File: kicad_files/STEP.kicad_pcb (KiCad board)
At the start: 2 copper layers, 12 x 20 mm, 39 parts, among them Q1 AOCA32116E, U1 STM32WB55CEU6TR, U2 LSM6DSO32TR, U3 ANT016008LCS2442MA2, U4 BQ297xy, U5 TPS62840DLCR, Y1 NX1612SA-32.000MHZ-CHP-CIS-3

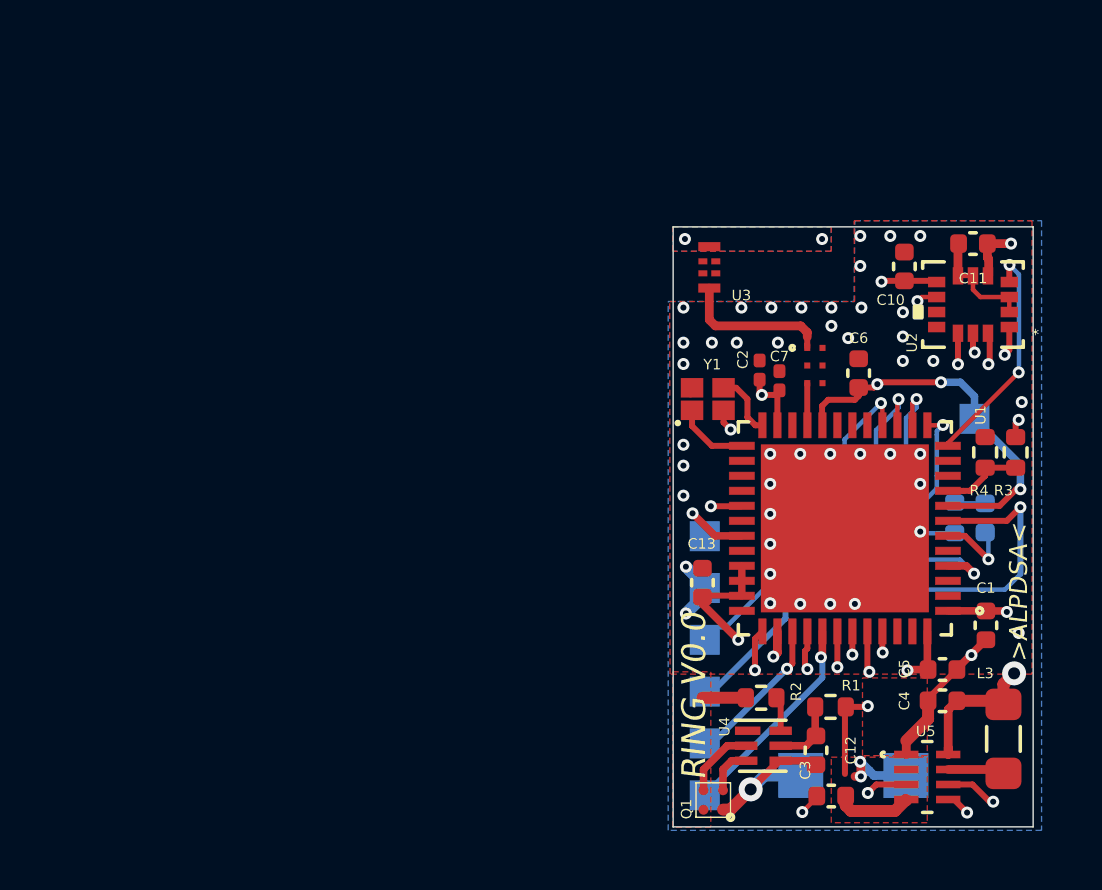
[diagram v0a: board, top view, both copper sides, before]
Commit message: finished v0.9 schematic and layout, annotated for review
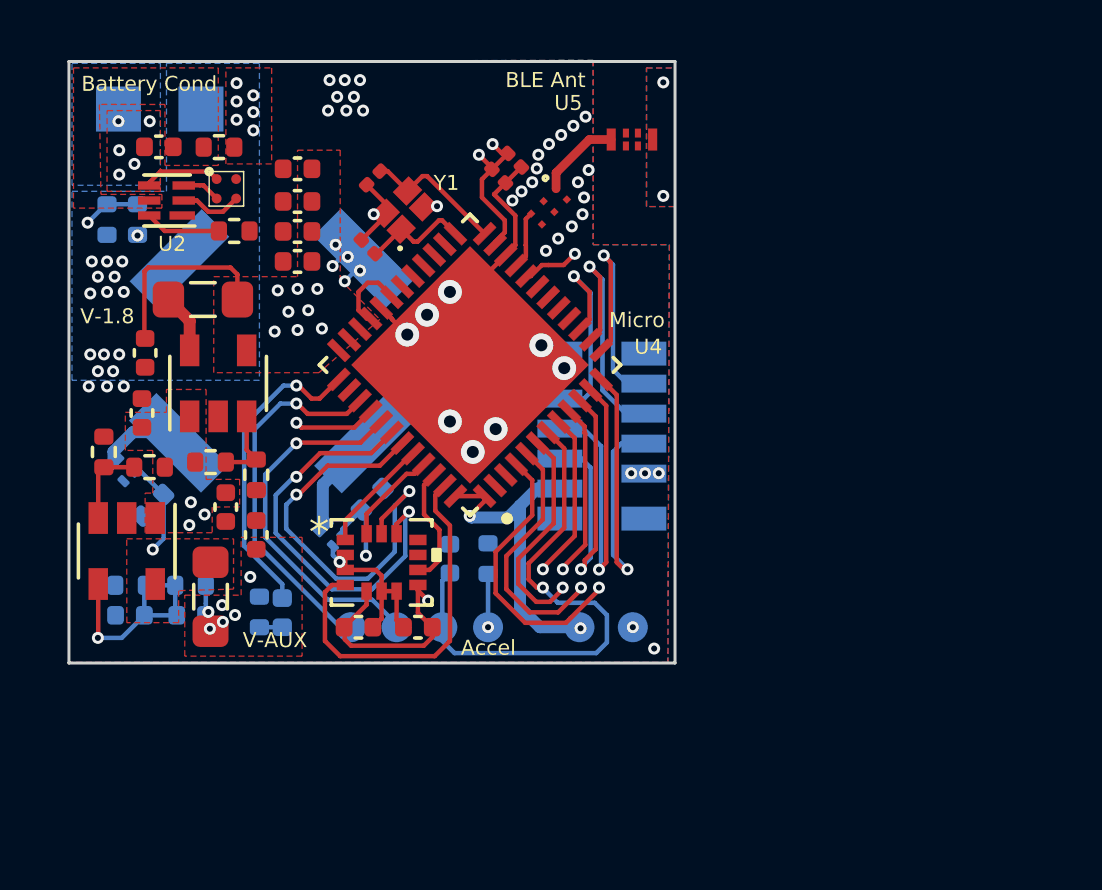
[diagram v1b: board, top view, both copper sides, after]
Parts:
- removed L3: L_2.2uH, Inductor_SMD:L_0805_2012Metric_Pad1.05x1.20mm_HandSolder
- removed TP10, TP11, TP12, TP13, TP9: Test_Point_SMD, TestPoint:TestPoint_Pad_1.0x1.0mm
- added C14: C_100nF, Capacitor_SMD:C_0402_1005Metric, F.Cu at (33.0, 32.0)
- added C15: C_4.7uF, Capacitor_SMD:C_0402_1005Metric, F.Cu at (30.6, 40.1)
- added C16: C_XF, Capacitor_SMD:C_0402_1005Metric, B.Cu at (29.5, 43.7)
- added C17: C_XF, Capacitor_SMD:C_0402_1005Metric, B.Cu at (27.4, 43.7)
- added C18: C_10uF, Capacitor_SMD:C_0402_1005Metric, F.Cu at (31.6, 41.1)
- added C8: C_100pF, Capacitor_SMD:C_0201_0603Metric, F.Cu at (35.5, 29.2)
- added C9: C_100nF, Capacitor_SMD:C_0402_1005Metric, F.Cu at (33.0, 28.9)
- added J1: CONN_FFC_FPC_VERT_8POS_0.5MM_SMD, step_footprints:tbf, B.Cu at (43.3, 37.8)
- added L1: L_2.2uH, Inductor_SMD:L_0805_2012Metric_Pad1.05x1.20mm_HandSolder, F.Cu at (29.9, 33.2)
- added L2: L_2.2uH, Inductor_SMD:L_0805_2012Metric_Pad1.05x1.20mm_HandSolder, F.Cu at (30.1, 43.1)
- added Q2: SSM3K35CTC, Package_TO_SOT_SMD:SOT-883, B.Cu at (34.1, 41.0)
- added Q3: SSM3K35CTC, Package_TO_SOT_SMD:SOT-883, B.Cu at (27.1, 38.9)
- added R10: R_10K, Resistor_SMD:R_0402_1005Metric, B.Cu at (39.4, 41.9)
- added R11: R_10K, Resistor_SMD:R_0402_1005Metric, B.Cu at (35.5, 39.9)
- added R12: R_10K, Resistor_SMD:R_0402_1005Metric, B.Cu at (28.2, 40.1)
- added R13: R_10k, Resistor_SMD:R_0402_1005Metric, F.Cu at (28.1, 38.8)
- added R14: R_X, Resistor_SMD:R_0402_1005Metric, F.Cu at (26.6, 38.3)
- added R15: R_10k, Resistor_SMD:R_0402_1005Metric, F.Cu at (30.1, 38.6)
- added R16: R_X, Resistor_SMD:R_0402_1005Metric, F.Cu at (31.6, 39.1)
- added R17: R_10k, Resistor_SMD:R_0402_1005Metric, B.Cu at (29.4, 42.7)
- added R18: R_X, Resistor_SMD:R_0402_1005Metric, B.Cu at (27.4, 42.7)
- added U6, U8: PKMCS0909E4000-R1, step_footprints:SPKR_PKMCS0909E4000-R1, B.Cu at (32.1, 34.9)
- added U7: LM3671TL-ADJ/NOPB, step_footprints:SOT-23-5, F.Cu at (27.3, 41.6)
- AE1: footprint step-footprints:MLPF-WB55-01E3 -> step_footprints:MLPF-WB55-01E3
- C1: value C_100nF -> C_4.7uF
- C11, C6: value C_100nF -> C_100pF; footprint Capacitor_SMD:C_0402_1005Metric -> Capacitor_SMD:C_0201_0603Metric
- C12: value C_0.1uF -> C_100nF
- C13: footprint Capacitor_SMD:C_0402_1005Metric -> Capacitor_SMD:C_0201_0603Metric
- C2: value C_100nF -> C_0.1uF; footprint Capacitor_SMD:C_0201_0603Metric -> Capacitor_SMD:C_0402_1005Metric
- C3: value C_4.7uF -> C_100nF
- C4: value C_10uF -> C_100nF
- C5: value C_100nF -> C_10uF
- C7: value C_100pF -> C_10nF; footprint Capacitor_SMD:C_0201_0603Metric -> Capacitor_SMD:C_0402_1005Metric; moved to B.Cu
- Q1: footprint step-footprints:AOCA32116E -> step_footprints:AOCA32116E
- R3, R4: moved to B.Cu
- TP1, TP2: footprint TestPoint:TestPoint_Pad_1.0x1.0mm -> TestPoint:TestPoint_Pad_1.5x1.5mm
- TP3, TP4, TP5, TP6: footprint TestPoint:TestPoint_Pad_1.0x1.0mm -> TestPoint:TestPoint_Pad_D1.0mm
- TP7, TP8: footprint TestPoint:TestPoint_Pad_1.5x1.5mm -> TestPoint:TestPoint_Pad_D1.0mm
- U1: value STM32WB55CEU6TR -> LSM6DSO32TR; footprint step-footprints:QFN50P700X700X60-49N -> step_footprints:LSM6DSO32TR
- U2: value LSM6DSO32TR -> BQ297xy; footprint step-footprints:LSM6DSO32TR -> Package_SON:WSON-6_1.5x1.5mm_P0.5mm
- U3: value ANT016008LCS2442MA2 -> LM3671TL-1V8/NOPB; footprint step-footprints:ANT016008LCS2442MA2 -> step_footprints:SOT-23-5
- U4: value BQ297xy -> STM32WB55CEU6TR; footprint Package_SON:WSON-6_1.5x1.5mm_P0.5mm -> step_footprints:QFN50P700X700X60-49N
- U5: value TPS62840DLCR -> ANT016008LCS2442MA2; footprint step-footprints:TPS62840DLCR -> step_footprints:ANT016008LCS2442MA2
- Y1: footprint step-footprints:OSCSC105P160X120X35-4N -> step_footprints:OSCSC105P160X120X35-4N
- moved R3 31.3 mm to (26.7, 30.6), turned to 90 degrees
- moved R4 29.3 mm to (27.7, 30.6), turned to -90 degrees
- moved C1 29.0 mm to (27.8, 37.0), turned to 90 degrees
- moved TP1 28.8 mm to (27.0, 26.9), turned to 180 degrees
- moved C5 28.6 mm to (27.9, 35.0), turned to -90 degrees
- moved TP2 28.4 mm to (29.8, 26.9), turned to 180 degrees
- moved R1 27.6 mm to (30.4, 28.1)
- moved U2 27.1 mm to (28.6, 29.9)
- moved Q1 26.5 mm to (30.3, 29.5), turned to -90 degrees
- moved C12 24.5 mm to (33.0, 31.0), turned to 180 degrees
- moved D1 23.6 mm to (32.5, 43.7), turned to 90 degrees
- moved R2 23.5 mm to (30.9, 30.9), turned to 180 degrees
- moved U5 23.4 mm to (44.2, 27.9), turned to 180 degrees
- moved R5 23.4 mm to (31.7, 43.6), turned to 90 degrees
- moved C2 21.4 mm to (28.4, 28.1), turned to 180 degrees
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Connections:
- AE1 pad 1: (no net) -> /RF_FILT
- AE1 pad 2: (no net) -> GND
- AE1 pad 3: (no net) -> /RF1
- AE1 pad 4: (no net) -> GND
- AE1 pad 5: (no net) -> GND
- AE1 pad 6: (no net) -> GND
- C1 pad 1: (no net) -> +BATT
- C1 pad 2: (no net) -> GND
- C10 pad 1: (no net) -> +1V8
- C10 pad 2: (no net) -> GND
- C11 pad 1: (no net) -> +1V8
- C11 pad 2: (no net) -> GND
- C12 pad 1: (no net) -> +1V8
- C12 pad 2: (no net) -> GND
- C13 pad 1: (no net) -> +1V8
- C13 pad 2: (no net) -> GND
- C2 pad 1: (no net) -> /BATT_FILT
- C2 pad 2: (no net) -> /CELL-
- C3 pad 1: (no net) -> +1V8
- C3 pad 2: (no net) -> GND
- C4 pad 1: (no net) -> +1V8
- C4 pad 2: (no net) -> GND
- C5 pad 1: (no net) -> +1V8
- C5 pad 2: (no net) -> GND
- C6 pad 1: (no net) -> /XTAL_FILT1
- C6 pad 2: (no net) -> GND
- C7 pad 1: (no net) -> /NRST
- C7 pad 2: (no net) -> GND
- D1 pad 1: (no net) -> Net-(D1-Pad1)
- D1 pad 2: (no net) -> /LED_DEBUG
- Q1 pad 1: (no net) -> /CELL-
- Q1 pad 2: (no net) -> GND
- Q1 pad 3: (no net) -> /C_GATE
- Q1 pad 4: (no net) -> /D_GATE
- R1 pad 1: (no net) -> /BATT_FILT
- R1 pad 2: (no net) -> +BATT
- R2 pad 1: (no net) -> GND
- R2 pad 2: (no net) -> /V_SENSE-
- R3 pad 1: (no net) -> +BATT
- R3 pad 2: (no net) -> /BATT_LVL
- R4 pad 1: (no net) -> /BATT_LVL
- R4 pad 2: (no net) -> GND
- R5 pad 1: (no net) -> Net-(D1-Pad1)
- R5 pad 2: (no net) -> GND
- TP1 pad 1: (no net) -> /CELL-
- TP2 pad 1: (no net) -> +BATT
- TP3 pad 1: (no net) -> /NRST
- TP4 pad 1: (no net) -> /SWDIO
- TP5 pad 1: (no net) -> /SWCLK
- TP6 pad 1: (no net) -> /BOOT0
- TP7 pad 1: (no net) -> +1V8
- TP8 pad 1: (no net) -> GND
- U1 pad 1: (no net) -> /MISO
- U1 pad 10: (no net) -> unconnected-(U1-Pad10)
- U1 pad 11: (no net) -> unconnected-(U1-Pad11)
- U1 pad 12: (no net) -> /CS
- U1 pad 13: (no net) -> /SCK
- U1 pad 14: (no net) -> /MOSI
- U1 pad 2: (no net) -> GND
- U1 pad 3: (no net) -> GND
- U1 pad 4: (no net) -> /LSM_INT1
- U1 pad 5: (no net) -> +1V8
- U1 pad 6: (no net) -> GND
- U1 pad 7: (no net) -> GND
- U1 pad 8: (no net) -> +1V8
- U1 pad 9: (no net) -> /LSM_INT2
- U2 pad 1: (no net) -> unconnected-(U2-Pad1)
- U2 pad 2: (no net) -> /C_GATE
- U2 pad 3: (no net) -> /D_GATE
- U2 pad 4: (no net) -> /CELL-
- U2 pad 5: (no net) -> /BATT_FILT
- U2 pad 6: (no net) -> /V_SENSE-
- U3 pad 1: (no net) -> +BATT
- U3 pad 2: (no net) -> GND
- U3 pad 3: (no net) -> /VEN_1V8
- U3 pad 4: (no net) -> +1V8
- U3 pad 5: (no net) -> /VSW_1V8
- U4 pad 1: (no net) -> +1V8
- U4 pad 2: (no net) -> unconnected-(U4-Pad2)
- U4 pad 3: (no net) -> unconnected-(U4-Pad3)
- U4 pad 4: (no net) -> /BOOT0
- U4 pad 5: (no net) -> /VBATT_BUZZER_LSD
- U4 pad 6: (no net) -> /VAUX_BUZZER_LSD
- U5 pad 1: (no net) -> /RAD_PLANE
- U5 pad 2: (no net) -> unconnected-(U5-Pad2)
- U5 pad 3: (no net) -> unconnected-(U5-Pad3)
- U5 pad 4: (no net) -> /RF_FILT
- U5 pad 5: (no net) -> unconnected-(U5-Pad5)
- U5 pad 6: (no net) -> unconnected-(U5-Pad6)
- Y1 pad 1: (no net) -> /XTAL_FILT1
- Y1 pad 2: (no net) -> GND
- Y1 pad 3: (no net) -> /XTAL_FILT3
- Y1 pad 4: (no net) -> GND
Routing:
- net (no net): track 180.9 -> 0.00 mm, vias 92 -> 0
- net +1V8: track 0.00 -> 48.3 mm, vias 0 -> 16
- net /BATT_LVL: track 0.00 -> 46.4 mm, vias 0 -> 3
- net /VAUX_BUZZER_LSD: track 0.00 -> 30.3 mm, vias 0 -> 2
- net /VBATT_BUZZER_LSD: track 0.00 -> 28.5 mm, vias 0 -> 2
- net GND: track 0.00 -> 21.0 mm, vias 0 -> 48
- net /NRST: track 0.00 -> 17.8 mm, vias 0 -> 1
- net /BOOT0: track 0.00 -> 17.2 mm, vias 0 -> 2
- net /SCK: track 0.00 -> 14.2 mm, vias 0 -> 2
- net /CS: track 0.00 -> 14.0 mm, vias 0 -> 2
- net /LSM_INT1: track 0.00 -> 12.5 mm
- net /SWCLK: track 0.00 -> 12.4 mm, vias 0 -> 1
- net /SWDIO: track 0.00 -> 12.3 mm, vias 0 -> 1
- net /ADC_IN_1: track 0.00 -> 12.1 mm, vias 0 -> 1
- net /ADC_IN_2: track 0.00 -> 12.0 mm, vias 0 -> 1
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- added copper zone on F.Cu, net +1V8
- added copper zone on In2.Cu, net +1V8
- added copper zone on B.Cu, net +BATT
- added copper zone on F.Cu, net +BATT
- added copper zone on In1.Cu, net +BATT
- added copper zone on F.Cu, net /BATT_FILT
- added copper zone on B.Cu, net /CELL-
- added copper zone on F.Cu, net /CELL-
- added copper zone on B.Cu, net /RAD_PLANE
- added copper zone on F.Cu, net /RAD_PLANE
- added copper zone on In1.Cu, net /RAD_PLANE
- added copper zone on In2.Cu, net /RAD_PLANE
- added copper zone on F.Cu, net /VSW_AUX
- added copper zone on B.Cu, net GND
- added copper zone on F.Cu, net GND
- added copper zone on In1.Cu, net GND
- added copper zone on In2.Cu, net GND
- added copper zone on F.Cu, net VAUX
- added copper zone on In1.Cu, net VAUX
- removed copper zone on B.Cu, net (none)
- removed copper zone on F.Cu, net (none)
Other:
- board size 12 x 20 mm -> 20.2 x 20.1 mm
- copper layers 2 -> 4
- board text added: "1.8V"
- board text added: "AUX Buzzer"
- board text added: "Accel"
- board text added: "BLE Ant"
- board text added: "Batt Buzzer"
- board text added: "Battery Cond"
- board text added: "CELL"
- board text added: "Haptic + Control Rev 0.9 - 3.10.23"
- board text added: "Micro"
- board text added: "NRST"
- board text added: "SWCLK"
- board text added: "SWDIO"
- board text added: "V-1.8"
- board text added: "V-AUX"
- board text added: "{dblquote}You have time to sleep when you're dead{dblquote}"
- board text removed: "1V8"
- board text removed: ">ALPDSA<"
- board text removed: "B0"
- board text removed: "B1"
- board text removed: "B2"
- board text removed: "B3"
- board text removed: "CLK"
- board text removed: "DIO"
- board text removed: "DNP"
- board text removed: "F ORII"
- board text removed: "RING V0.0"
- board text removed: "RST"
- board text removed: "[STEP AFTERHOURS]"
- board text removed: "~{NEON} RAINBOWS~{}"
- board text removed: "~{PCB} POLICE~{ }WAS HERE~{}"

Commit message: adjusted single via
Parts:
- C16: value C_XF -> C_YF
- R13, R15: value R_10k -> R_200k
- R14, R16: value R_X -> R_100k
- R17: value R_10k -> R_Y
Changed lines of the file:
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@@
       (effects (font (size 1 1) (thickness 0.15)))
     )
-    (fp_text value "R_X" (at 0 1.17 90) (layer "F.Fab")
+    (fp_text value "R_100k" (at 0 1.17 90) (layer "F.Fab")
       (effects (font (size 1 1) (thickness 0.15)))
     )
@@
       (effects (font (size 1 1) (thickness 0.15)))
     )
-    (fp_text value "R_X" (at 0 1.17 90) (layer "F.Fab")
+    (fp_text value "R_100k" (at 0 1.17 90) (layer "F.Fab")
       (effects (font (size 1 1) (thickness 0.15)))
     )
@@
       (effects (font (size 1 1) (thickness 0.15)))
     )
-    (fp_text value "R_10k" (at 0 1.17) (layer "F.Fab")
+    (fp_text value "R_200k" (at 0 1.17) (layer "F.Fab")
       (effects (font (size 1 1) (thickness 0.15)))
     )
@@
       (effects (font (size 1 1) (thickness 0.15)))
     )
-    (fp_text value "R_10k" (at 0 1.17) (layer "F.Fab")
+    (fp_text value "R_200k" (at 0 1.17) (layer "F.Fab")
       (effects (font (size 1 1) (thickness 0.15)))
     )
@@
       (effects (font (size 1 1) (thickness 0.15)) (justify mirror))
     )
-    (fp_text value "R_10k" (at 0 -1.17) (layer "B.Fab")
+    (fp_text value "R_Y" (at 0 -1.17) (layer "B.Fab")
       (effects (font (size 1 1) (thickness 0.15)) (justify mirror))
     )
@@
       (effects (font (size 1 1) (thickness 0.15)) (justify mirror))
     )
-    (fp_text value "C_XF" (at 0 -1.16) (layer "B.Fab")
-      (effects (font (size 1 1) (thickness 0.15)) (justify mirror))
-    )
+    (fp_text value "C_YF" (at 0 -1.16) (layer "B.Fab")
+      (effects (font (size 1 1) (thickness 0.15)) (justify mirror))
+    )

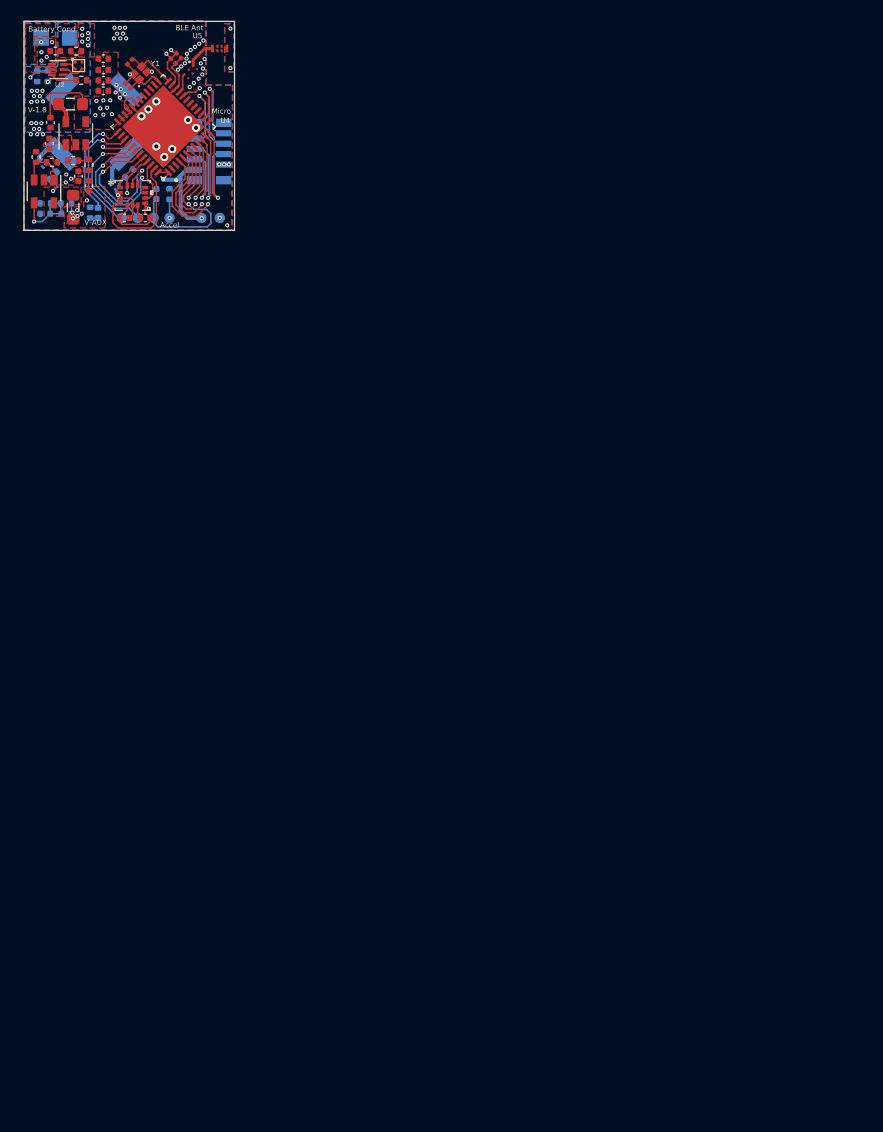
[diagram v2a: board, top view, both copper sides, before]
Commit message: post design review feedback, switching to external antenna for prototyping
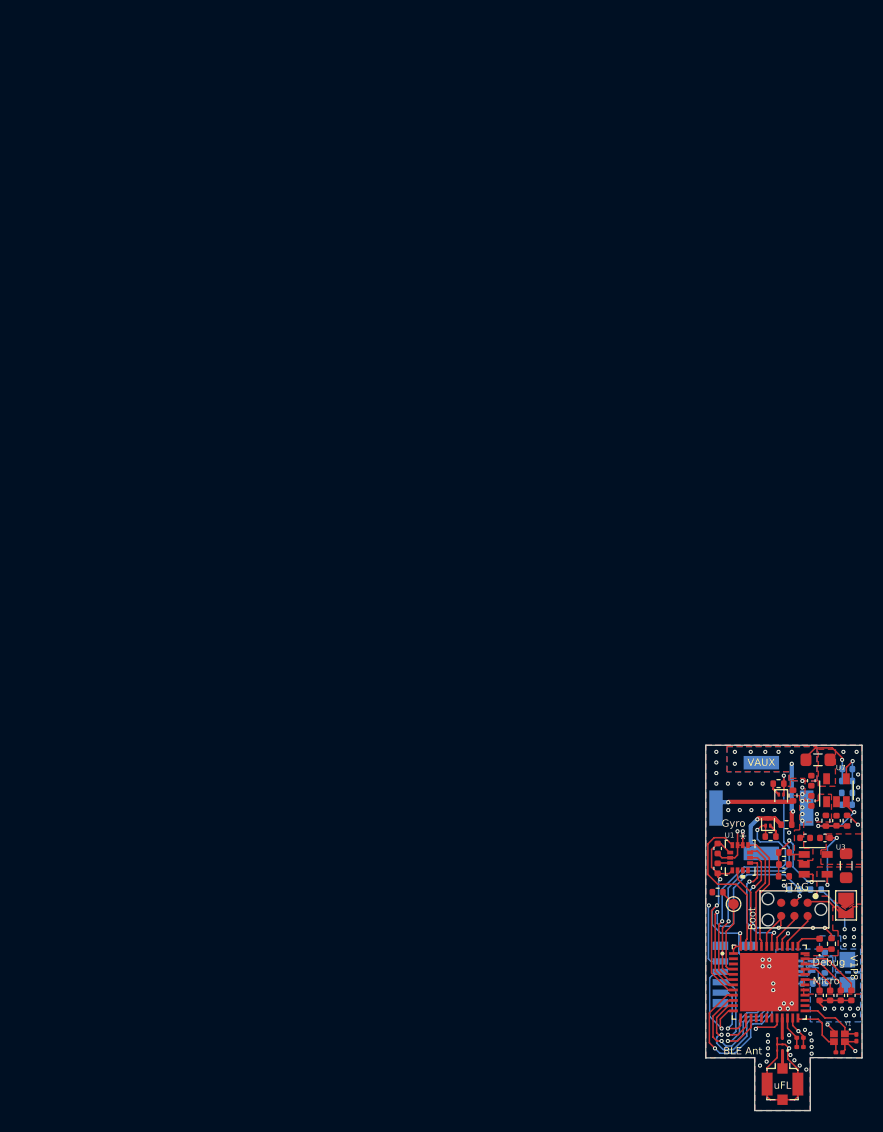
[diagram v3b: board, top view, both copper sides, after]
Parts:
- removed TP4, TP5, TP6, TP7, TP8: Test_Point_SMD, TestPoint:TestPoint_Pad_D1.0mm
- added C19: C_XF, Capacitor_SMD:C_0402_1005Metric, F.Cu at (103.3, 102.0)
- added C20: C_XF, Capacitor_SMD:C_0402_1005Metric, F.Cu at (98.3, 106.2)
- added J2: TC2030-IDC-TAGCONNECT, step_footprints:TAG_TC2030-IDC-NL, F.Cu at (99.3, 110.5)
- added R6: R_0, Jumper:SolderJumper-2_P1.3mm_Open_TrianglePad1.0x1.5mm, F.Cu at (104.3, 110.1)
- added R7: R_10K, Resistor_SMD:R_0402_1005Metric, F.Cu at (99.2, 99.6)
- added R8: R_10K, Resistor_SMD:R_0402_1005Metric, B.Cu at (101.4, 108.6)
- added R9: R_10K, Resistor_SMD:R_0402_1005Metric, F.Cu at (98.5, 102.4)
- C2, Q1, R1, R2, U2: moved to B.Cu
- D1, Q2, Q3, R10, R11, R12, R5, TP3: moved to F.Cu
- J1: value CONN_FFC_FPC_VERT_8POS_0.5MM_SMD -> Molex_FFC_FPC_VERT_8POS_0.5MM_SMD_0525590853
- U5: value ANT016008LCS2442MA2 -> Molex_Conn_uFL_0734120110; footprint step_footprints:ANT016008LCS2442MA2 -> Connector_Coaxial:U.FL_Molex_MCRF_73412-0110_Vertical
- moved TP2 117.6 mm to (104.4, 117.7)
- moved TP1 117.5 mm to (104.4, 115.3)
- moved C8 116.9 mm to (103.6, 124.2), turned to 0 degrees
- moved C6 115.0 mm to (105.3, 122.8), turned to -90 degrees
- moved C9 115.0 mm to (104.8, 118.7), turned to -90 degrees
- moved R1 114.3 mm to (102.2, 117.1), turned to -90 degrees
- moved Y1 114.3 mm to (103.6, 122.8), turned to 180 degrees
- moved R3 114.2 mm to (100.6, 117.6), turned to 180 degrees
- moved C2 114.1 mm to (102.2, 115.1), turned to 90 degrees
- moved C10 113.5 mm to (103.8, 118.7), turned to -90 degrees
- moved U5 113.1 mm to (98.2, 127.3)
- moved R4 112.5 mm to (98.6, 118.0), turned to 180 degrees
- moved C12 112.1 mm to (102.7, 118.7), turned to -90 degrees
- moved C11 112.1 mm to (99.9, 123.7), turned to 180 degrees
- moved U2 112.0 mm to (100.4, 115.9), turned to 0 degrees
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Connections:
- C5 pad 1: +1V8 -> /VFB_1V8
- L1 pad 2: +1V8 -> /VFB_1V8
- TP3 pad 1: /NRST -> /BOOT0
- U3 pad 4: +1V8 -> /VFB_1V8
- U4 pad 10: /ADC_IN_0 -> /ADC_IN_1
- U4 pad 11: /ADC_IN_1 -> /ADC_IN_0
- U5 pad 1: /RAD_PLANE -> /RF_FILT
- U5 pad 2: unconnected-(U5-Pad2) -> GND
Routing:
- net GND: track 21.0 -> 51.1 mm, vias 48 -> 57
- net /BATT_LVL: track 46.4 -> 19.7 mm, vias 3 -> 1
- net +1V8: track 48.3 -> 63.1 mm, vias 16 -> 12
- net VAUX: track 2.76 -> 12.7 mm, vias 11 -> 9
- net /SWCLK: track 12.4 -> 3.53 mm, vias 1 -> 0
- net /SWDIO: track 12.3 -> 3.64 mm, vias 1 -> 0
- net /BOOT0: track 17.2 -> 8.66 mm, vias 2 -> 0
- net /VEN_1V8: track 2.62 -> 10.5 mm, vias 0 -> 2
- net /LED_DEBUG: track 10.4 -> 2.57 mm, vias 1 -> 0
- net /MISO: track 3.83 -> 11.5 mm
- net /ADC_IN_0: track 10.7 -> 18.0 mm
- net /MOSI: track 3.25 -> 10.6 mm
- net /VFB_1V8: track 0.00 -> 6.55 mm, vias 0 -> 2
- net /NRST: track 17.8 -> 24.3 mm, vias 1 -> 2
- net /VAUX_BUZZER_LSD: track 30.3 -> 24.2 mm
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- added copper zone on B.Cu, net /BATT_FILT
- added copper zone on F.Cu, net /VFB_1V8
- added copper zone on F.Cu, net /VSW_1V8
- added copper zone on B.Cu, net VAUX
- removed copper zone on F.Cu, net /BATT_FILT
- removed copper zone on F.Cu, net /CELL-
- removed copper zone on B.Cu, net /RAD_PLANE
- removed copper zone on F.Cu, net /RAD_PLANE
- removed copper zone on In1.Cu, net /RAD_PLANE
- removed copper zone on In2.Cu, net /RAD_PLANE
- removed copper zone on In1.Cu, net VAUX
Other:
- board size 20.2 x 20.1 mm -> 15 x 35.1 mm
- board text added: "0"
- board text added: "0 mm"
- board text added: "0.01 mm"
- board text added: "0.02"
- board text added: "0.035 mm"
- board text added: "1"
- board text added: "1.51 mm"
- board text added: "3.3"
- board text added: "4.5"
- board text added: "AUX"
- board text added: "B.Cu"
- board text added: "B.Mask"
- board text added: "B.Paste"
- board text added: "B.Silkscreen"
- board text added: "BATT"
- board text added: "Boot"
- board text added: "Bottom Silk Screen"
- board text added: "Bottom Solder Mask"
- board text added: "Bottom Solder Paste"
- board text added: "Color"
- board text added: "Debug"
- board text added: "Dielectric"
- board text added: "Epsilon R"
- board text added: "F.Cu"
- board text added: "F.Mask"
- board text added: "F.Paste"
- board text added: "F.Silkscreen"
- board text added: "FR4"
- board text added: "Gyro"
- board text added: "Haptics + Feeback Module STEP 2023 3.16.23"
- board text added: "In1.Cu"
- board text added: "In2.Cu"
- board text added: "JTAG"
- board text added: "Layer Name"
- board text added: "Loss Tangent"
- board text added: "Material"
- board text added: "Not specified"
- board text added: "Thickness (mm)"
- board text added: "Top Silk Screen"
- board text added: "Top Solder Mask"
- board text added: "Top Solder Paste"
- board text added: "Type"
- board text added: "V1P8"
- board text added: "VAUX"
- board text added: "copper"
- board text added: "core"
- board text added: "prepreg"
- board text added: "uFL"
- board text removed: "1.8V"
- board text removed: "AUX Buzzer"
- board text removed: "Accel"
- board text removed: "BOOT"
- board text removed: "Batt Buzzer"
- board text removed: "Battery Cond"
- board text removed: "GND"
- board text removed: "Haptic + Control Rev 0.9 - 3.10.23"
- board text removed: "NRST"
- board text removed: "SWCLK"
- board text removed: "SWDIO"
- board text removed: "V-1.8"
- board text removed: "V-AUX"
- board text removed: "{dblquote}You have time to sleep when you're dead{dblquote}"
